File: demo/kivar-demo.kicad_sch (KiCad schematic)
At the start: 0 parts

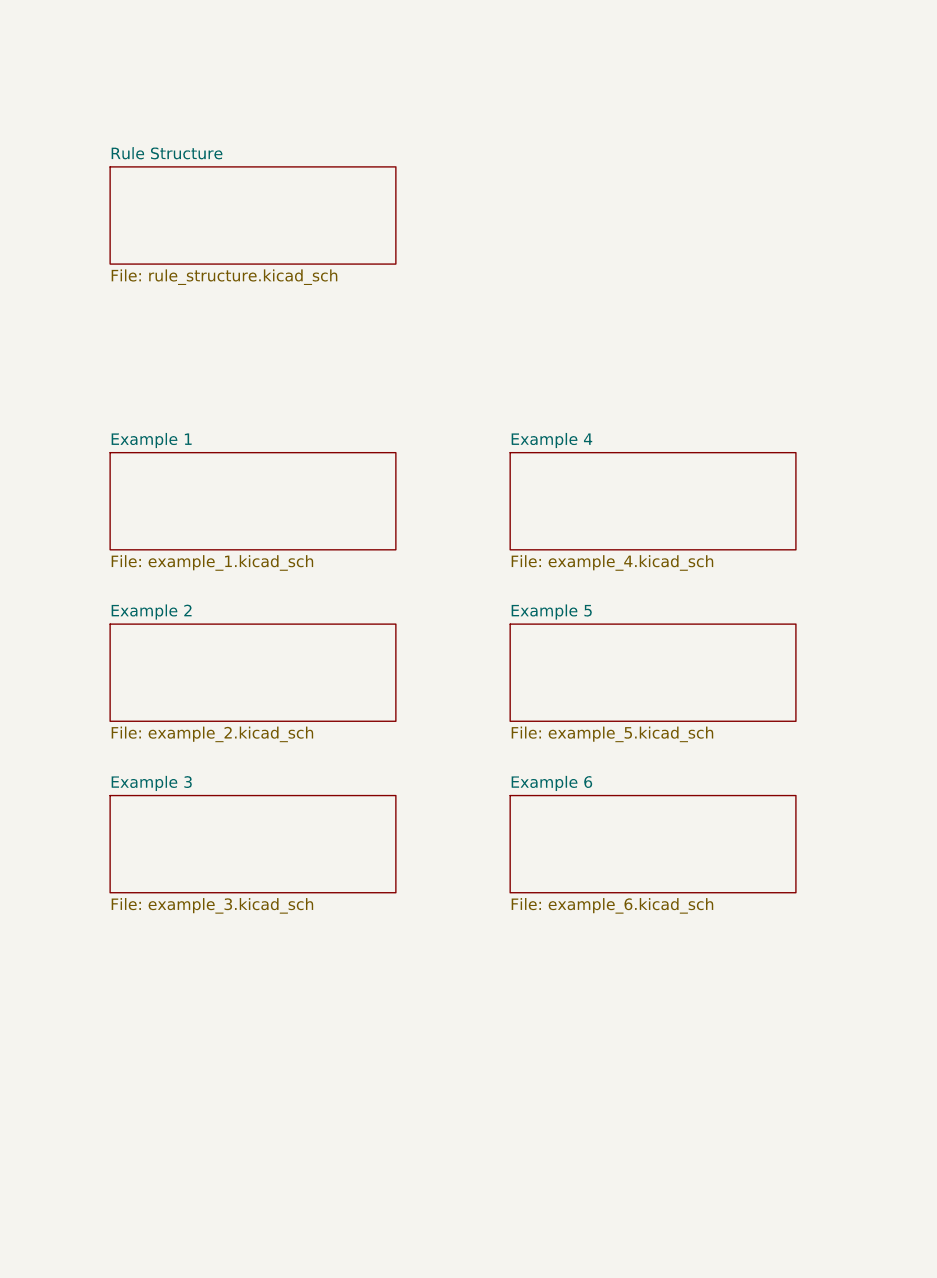
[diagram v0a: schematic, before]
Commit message: Use example descriptions on root sheet, refine block and text sizes
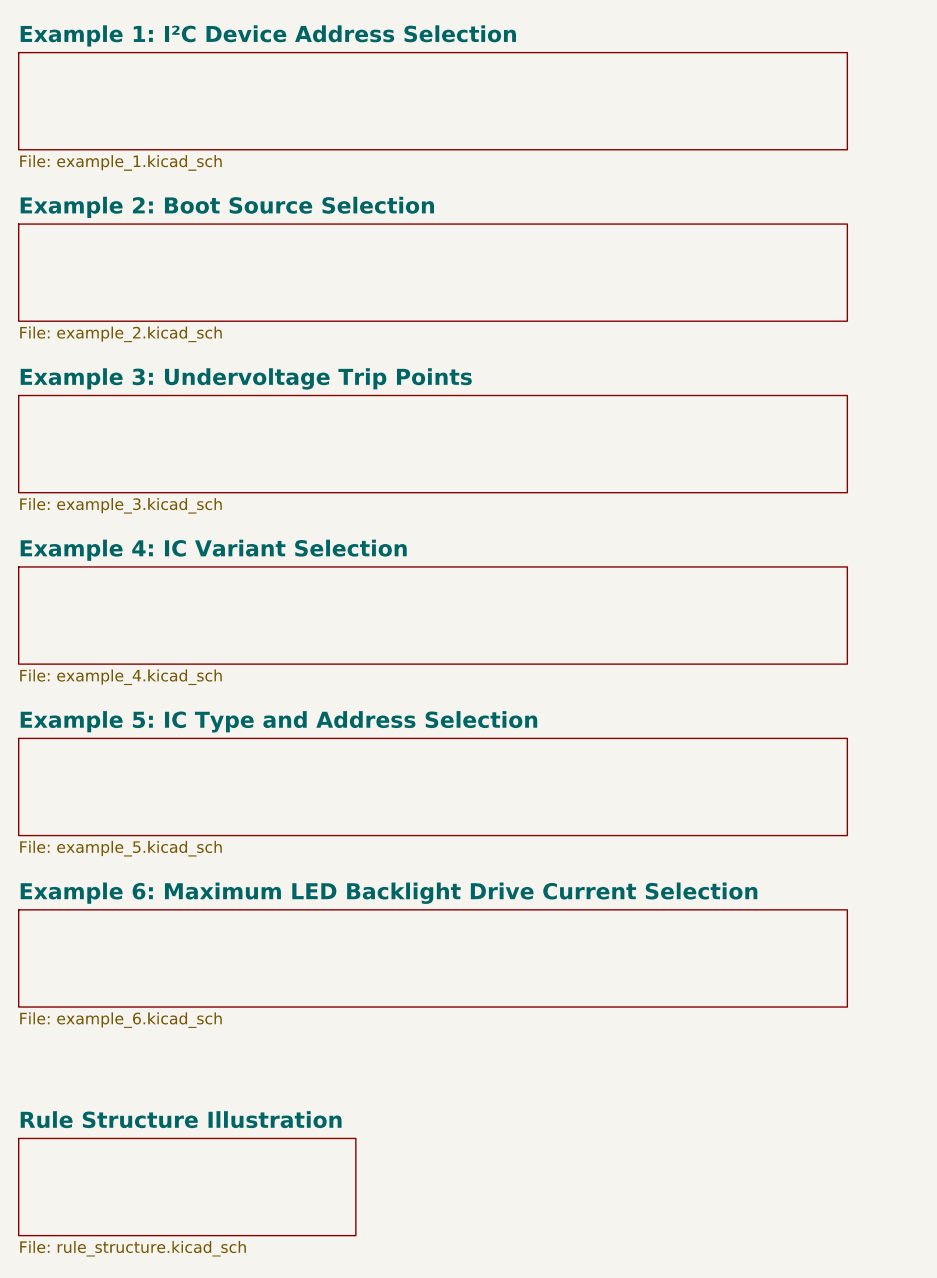
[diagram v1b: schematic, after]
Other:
- sheet Example 1 renamed Example 1: I²C Device Address Selection
- sheet Example 2 renamed Example 2: Boot Source Selection
- sheet Example 3 renamed Example 3: Undervoltage Trip Points
- sheet Example 4 renamed Example 4: IC Variant Selection
- sheet Example 5 renamed Example 5: IC Type and Address Selection
- sheet Example 6 renamed Example 6: Maximum LED Backlight Drive Current Selection
- sheet Rule Structure renamed Rule Structure Illustration
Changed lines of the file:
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@@
 	(title_block
 		(title "KiVar Demo")
-		(date "2024-01-16")
+		(date "2024-02-07")
 		(company "Author: Mark Hämmerling <dev@markh.de>")
 		(comment 1 "https://github.com/markh-de/KiVar")
@@
 	)
 	(sheet
-		(at 82.55 88.9)
-		(size 31.75 10.795)
-		(fields_autoplaced yes)
-		(stroke
-			(width 0.1524)
-			(type solid)
-		)
-		(fill
-			(color 255 229 191 1.0000)
-		)
-		(property "Sheetname" "Example 5"
-			(at 82.55 88.1884 0)
-			(effects
-				(font
-					(size 1.27 1.27)
+		(at 27.94 101.6)
+		(size 92.075 10.795)
+		(fields_autoplaced yes)
+		(stroke
+			(width 0.1524)
+			(type solid)
+		)
+		(fill
+			(color 255 229 191 1.0000)
+		)
+		(property "Sheetname" "Example 5: IC Type and Address Selection"
+			(at 27.94 100.6344 0)
+			(effects
+				(font
+					(size 1.778 1.778)
+					(bold yes)
 				)
 				(justify left bottom)
@@
 		)
 		(property "Sheetfile" "example_5.kicad_sch"
-			(at 82.55 100.2796 0)
+			(at 27.94 112.9796 0)
 			(effects
 				(font
@@
 	)
 	(sheet
-		(at 38.1 69.85)
-		(size 31.75 10.795)
-		(fields_autoplaced yes)
-		(stroke
-			(width 0.1524)
-			(type solid)
-		)
-		(fill
-			(color 255 229 191 1.0000)
-		)
-		(property "Sheetname" "Example 1"
-			(at 38.1 69.1384 0)
-			(effects
-				(font
-					(size 1.27 1.27)
+		(at 27.94 25.4)
+		(size 92.075 10.795)
+		(fields_autoplaced yes)
+		(stroke
+			(width 0.1524)
+			(type solid)
+		)
+		(fill
+			(color 255 229 191 1.0000)
+		)
+		(property "Sheetname" "Example 1: I²C Device Address Selection"
+			(at 27.94 24.4344 0)
+			(effects
+				(font
+					(size 1.778 1.778)
+					(bold yes)
 				)
 				(justify left bottom)
@@
 		)
 		(property "Sheetfile" "example_1.kicad_sch"
-			(at 38.1 81.2296 0)
+			(at 27.94 36.7796 0)
 			(effects
 				(font
@@
 	)
 	(sheet
-		(at 38.1 107.95)
-		(size 31.75 10.795)
-		(fields_autoplaced yes)
-		(stroke
-			(width 0.1524)
-			(type solid)
-		)
-		(fill
-			(color 255 229 191 1.0000)
-		)
-		(property "Sheetname" "Example 3"
-			(at 38.1 107.2384 0)
-			(effects
-				(font
-					(size 1.27 1.27)
+		(at 27.94 63.5)
+		(size 92.075 10.795)
+		(fields_autoplaced yes)
+		(stroke
+			(width 0.1524)
+			(type solid)
+		)
+		(fill
+			(color 255 229 191 1.0000)
+		)
+		(property "Sheetname" "Example 3: Undervoltage Trip Points"
+			(at 27.94 62.5344 0)
+			(effects
+				(font
+					(size 1.778 1.778)
+					(bold yes)
 				)
 				(justify left bottom)
@@
 		)
 		(property "Sheetfile" "example_3.kicad_sch"
-			(at 38.1 119.3296 0)
+			(at 27.94 74.8796 0)
 			(effects
 				(font
@@
 	)
 	(sheet
-		(at 82.55 69.85)
-		(size 31.75 10.795)
-		(fields_autoplaced yes)
-		(stroke
-			(width 0.1524)
-			(type solid)
-		)
-		(fill
-			(color 255 229 191 1.0000)
-		)
-		(property "Sheetname" "Example 4"
-			(at 82.55 69.1384 0)
-			(effects
-				(font
-					(size 1.27 1.27)
+		(at 27.94 82.55)
+		(size 92.075 10.795)
+		(fields_autoplaced yes)
+		(stroke
+			(width 0.1524)
+			(type solid)
+		)
+		(fill
+			(color 255 229 191 1.0000)
+		)
+		(property "Sheetname" "Example 4: IC Variant Selection"
+			(at 27.94 81.5844 0)
+			(effects
+				(font
+					(size 1.778 1.778)
+					(bold yes)
 				)
 				(justify left bottom)
@@
 		)
 		(property "Sheetfile" "example_4.kicad_sch"
-			(at 82.55 81.2296 0)
+			(at 27.94 93.9296 0)
 			(effects
 				(font
@@
 	)
 	(sheet
-		(at 38.1 38.1)
-		(size 31.75 10.795)
+		(at 27.94 146.05)
+		(size 37.465 10.795)
 		(fields_autoplaced yes)
 		(stroke
@@
 			(color 255 255 194 1.0000)
 		)
-		(property "Sheetname" "Rule Structure"
-			(at 38.1 37.3884 0)
-			(effects
-				(font
-					(size 1.27 1.27)
+		(property "Sheetname" "Rule Structure Illustration"
+			(at 27.94 145.0844 0)
+			(effects
+				(font
+					(size 1.778 1.778)
+					(bold yes)
 				)
 				(justify left bottom)
@@
 		)
 		(property "Sheetfile" "rule_structure.kicad_sch"
-			(at 38.1 49.4796 0)
+			(at 27.94 157.4296 0)
 			(effects
 				(font
@@
 	)
 	(sheet
-		(at 82.55 107.95)
-		(size 31.75 10.795)
-		(fields_autoplaced yes)
-		(stroke
-			(width 0.1524)
-			(type solid)
-		)
-		(fill
-			(color 255 229 191 1.0000)
-		)
-		(property "Sheetname" "Example 6"
-			(at 82.55 107.2384 0)
-			(effects
-				(font
-					(size 1.27 1.27)
+		(at 27.94 120.65)
+		(size 92.075 10.795)
+		(fields_autoplaced yes)
+		(stroke
+			(width 0.1524)
+			(type solid)
+		)
+		(fill
+			(color 255 229 191 1.0000)
+		)
+		(property "Sheetname" "Example 6: Maximum LED Backlight Drive Current Selection"
+			(at 27.94 119.6844 0)
+			(effects
+				(font
+					(size 1.778 1.778)
+					(bold yes)
 				)
 				(justify left bottom)
@@
 		)
 		(property "Sheetfile" "example_6.kicad_sch"
-			(at 82.55 119.3296 0)
+			(at 27.94 132.0296 0)
 			(effects
 				(font
@@
 	)
 	(sheet
-		(at 38.1 88.9)
-		(size 31.75 10.795)
-		(fields_autoplaced yes)
-		(stroke
-			(width 0.1524)
-			(type solid)
-		)
-		(fill
-			(color 255 229 191 1.0000)
-		)
-		(property "Sheetname" "Example 2"
-			(at 38.1 88.1884 0)
-			(effects
-				(font
-					(size 1.27 1.27)
+		(at 27.94 44.45)
+		(size 92.075 10.795)
+		(fields_autoplaced yes)
+		(stroke
+			(width 0.1524)
+			(type solid)
+		)
+		(fill
+			(color 255 229 191 1.0000)
+		)
+		(property "Sheetname" "Example 2: Boot Source Selection"
+			(at 27.94 43.4844 0)
+			(effects
+				(font
+					(size 1.778 1.778)
+					(bold yes)
 				)
 				(justify left bottom)
@@
 		)
 		(property "Sheetfile" "example_2.kicad_sch"
-			(at 38.1 100.2796 0)
-			(effects
-				(font
+			(at 27.94 55.8296 0)
+			(effects
+				(font

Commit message: Add rule compiler illustration, use fancier colors
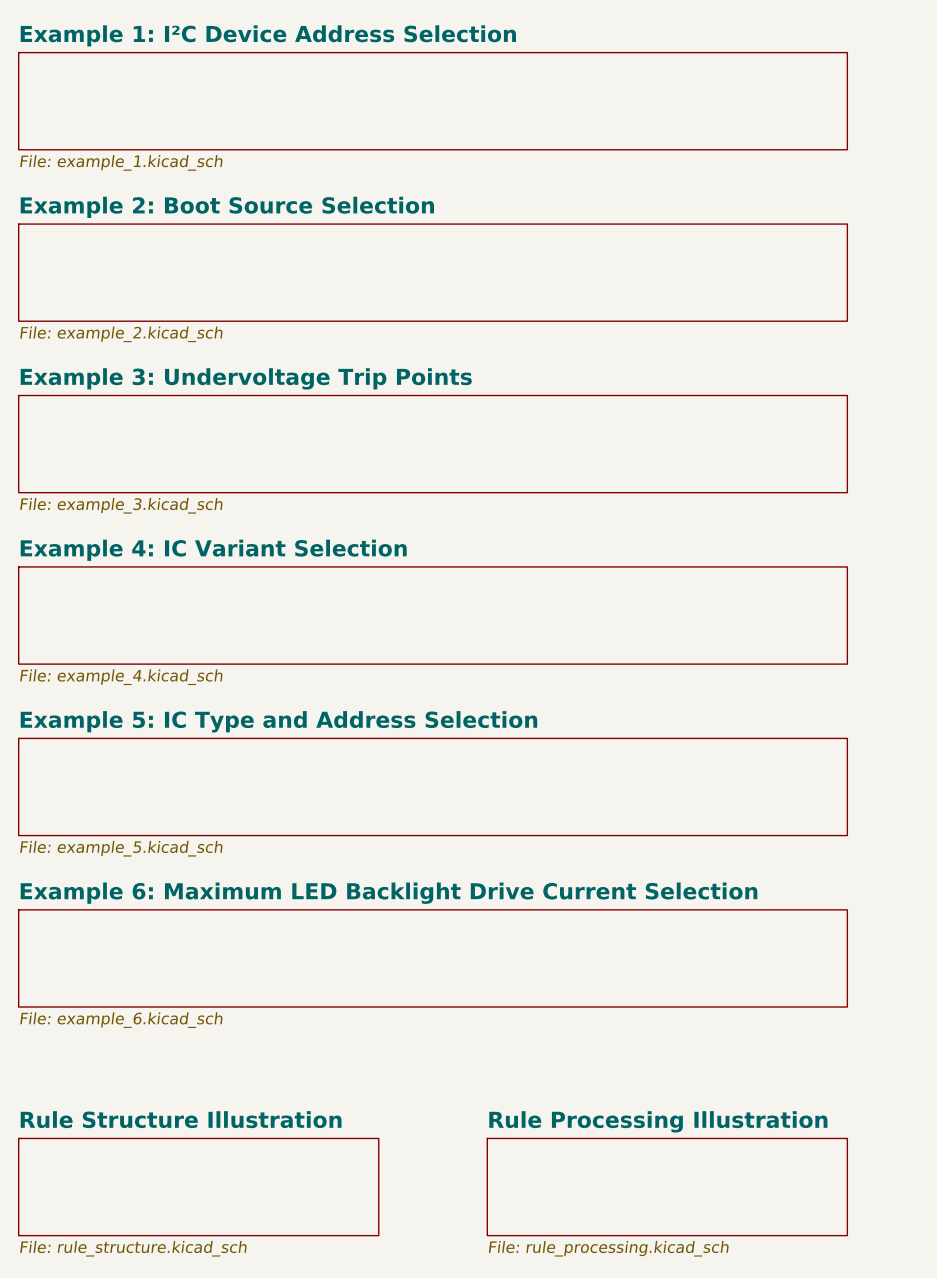
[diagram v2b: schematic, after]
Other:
- added sheet Rule Processing Illustration (rule_processing.kicad_sch)
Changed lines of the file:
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@@
 	(title_block
 		(title "KiVar Demo")
-		(date "2024-02-07")
+		(date "2024-02-10")
 		(company "Author: Mark Hämmerling <dev@markh.de>")
 		(comment 1 "https://github.com/markh-de/KiVar")
@@
 			(width 0.1524)
 			(type solid)
-		)
-		(fill
-			(color 255 229 191 1.0000)
+			(color 125 147 158 1)
+		)
+		(fill
+			(color 181 212 228 1.0000)
 		)
 		(property "Sheetname" "Example 5: IC Type and Address Selection"
@@
 					(size 1.778 1.778)
 					(bold yes)
+					(color 146 108 108 1)
 				)
 				(justify left bottom)
@@
 				(font
 					(size 1.27 1.27)
+					(italic yes)
+					(color 194 194 194 1)
 				)
 				(justify left top)
@@
 	)
 	(sheet
+		(at 80.01 146.05)
+		(size 40.005 10.795)
+		(fields_autoplaced yes)
+		(stroke
+			(width 0.1524)
+			(type solid)
+			(color 151 166 142 1)
+		)
+		(fill
+			(color 208 229 196 1.0000)
+		)
+		(property "Sheetname" "Rule Processing Illustration"
+			(at 80.01 145.0844 0)
+			(effects
+				(font
+					(size 1.778 1.778)
+					(bold yes)
+					(color 146 108 108 1)
+				)
+				(justify left bottom)
+			)
+		)
+		(property "Sheetfile" "rule_processing.kicad_sch"
+			(at 80.01 157.4296 0)
+			(effects
+				(font
+					(size 1.27 1.27)
+					(italic yes)
+					(color 194 194 194 1)
+				)
+				(justify left top)
+			)
+		)
+		(instances
+			(project "kivar-demo"
+				(path "/cd745a5c-45fb-4106-85c8-c86c130b6ee7"
+					(page "9")
+				)
+			)
+		)
+	)
+	(sheet
 		(at 27.94 25.4)
 		(size 92.075 10.795)
@@
 			(width 0.1524)
 			(type solid)
-		)
-		(fill
-			(color 255 229 191 1.0000)
+			(color 125 147 158 1)
+		)
+		(fill
+			(color 181 212 228 1.0000)
 		)
 		(property "Sheetname" "Example 1: I²C Device Address Selection"
@@
 					(size 1.778 1.778)
 					(bold yes)
+					(color 146 108 108 1)
 				)
 				(justify left bottom)
@@
 				(font
 					(size 1.27 1.27)
+					(italic yes)
+					(color 194 194 194 1)
 				)
 				(justify left top)
@@
 			(width 0.1524)
 			(type solid)
-		)
-		(fill
-			(color 255 229 191 1.0000)
+			(color 125 147 158 1)
+		)
+		(fill
+			(color 181 212 228 1.0000)
 		)
 		(property "Sheetname" "Example 3: Undervoltage Trip Points"
@@
 					(size 1.778 1.778)
 					(bold yes)
+					(color 146 108 108 1)
 				)
 				(justify left bottom)
@@
 				(font
 					(size 1.27 1.27)
+					(italic yes)
+					(color 194 194 194 1)
 				)
 				(justify left top)
@@
 			(width 0.1524)
 			(type solid)
-		)
-		(fill
-			(color 255 229 191 1.0000)
+			(color 125 147 158 1)
+		)
+		(fill
+			(color 181 212 228 1.0000)
 		)
 		(property "Sheetname" "Example 4: IC Variant Selection"
@@
 					(size 1.778 1.778)
 					(bold yes)
+					(color 146 108 108 1)
 				)
 				(justify left bottom)
@@
 				(font
 					(size 1.27 1.27)
+					(italic yes)
+					(color 194 194 194 1)
 				)
 				(justify left top)
@@
 	(sheet
 		(at 27.94 146.05)
-		(size 37.465 10.795)
-		(fields_autoplaced yes)
-		(stroke
-			(width 0.1524)
-			(type solid)
-		)
-		(fill
-			(color 255 255 194 1.0000)
+		(size 40.005 10.795)
+		(fields_autoplaced yes)
+		(stroke
+			(width 0.1524)
+			(type solid)
+			(color 151 166 142 1)
+		)
+		(fill
+			(color 208 229 196 1.0000)
 		)
 		(property "Sheetname" "Rule Structure Illustration"
@@
 					(size 1.778 1.778)
 					(bold yes)
+					(color 146 108 108 1)
 				)
 				(justify left bottom)
@@
 				(font
 					(size 1.27 1.27)
+					(italic yes)
+					(color 194 194 194 1)
 				)
 				(justify left top)
@@
 			(width 0.1524)
 			(type solid)
-		)
-		(fill
-			(color 255 229 191 1.0000)
+			(color 125 147 158 1)
+		)
+		(fill
+			(color 181 212 228 1.0000)
 		)
 		(property "Sheetname" "Example 6: Maximum LED Backlight Drive Current Selection"
@@
 					(size 1.778 1.778)
 					(bold yes)
+					(color 146 108 108 1)
 				)
 				(justify left bottom)
@@
 				(font
 					(size 1.27 1.27)
+					(italic yes)
+					(color 194 194 194 1)
 				)
 				(justify left top)
@@
 			(width 0.1524)
 			(type solid)
-		)
-		(fill
-			(color 255 229 191 1.0000)
+			(color 125 147 158 1)
+		)
+		(fill
+			(color 181 212 228 1.0000)
 		)
 		(property "Sheetname" "Example 2: Boot Source Selection"
@@
 					(size 1.778 1.778)
 					(bold yes)
+					(color 146 108 108 1)
 				)
 				(justify left bottom)
@@
 				(font
 					(size 1.27 1.27)
-				)
-				(justify left top)
+					(italic yes)
+					(color 194 194 194 1)
+				)
+				(justify left top)
